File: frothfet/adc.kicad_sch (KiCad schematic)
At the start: 5 parts, among them U18 MCP3564R

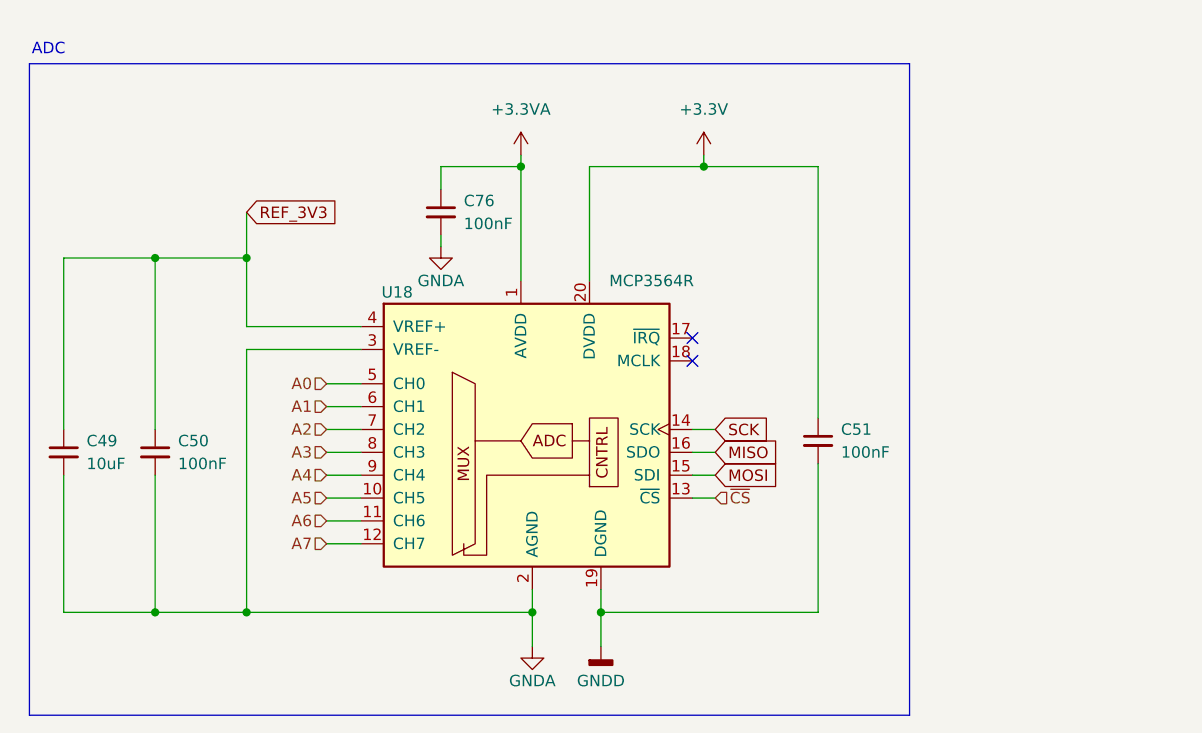
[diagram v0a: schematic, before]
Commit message: fatter power trace and layer 3 is fully ground plane now.
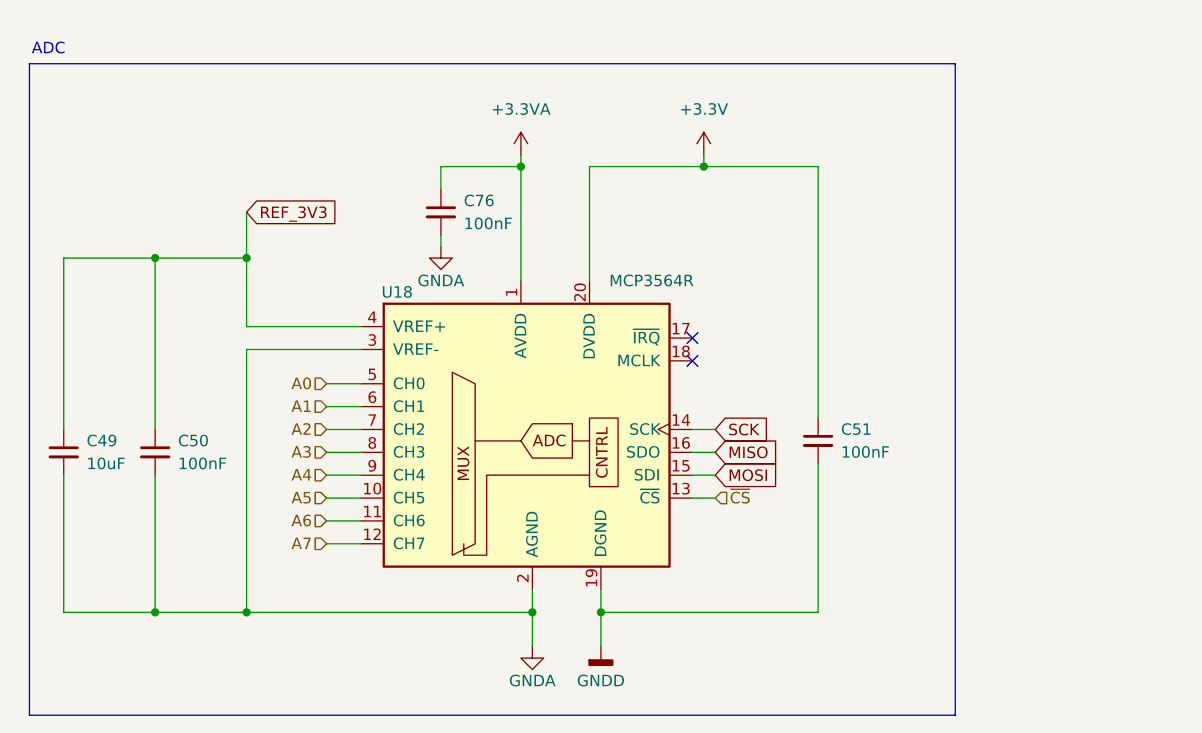
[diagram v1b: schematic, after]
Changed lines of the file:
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@@
 	(rectangle
 		(start 81.28 45.72)
-		(end 179.07 118.11)
+		(end 184.15 118.11)
 		(stroke
 			(width 0)

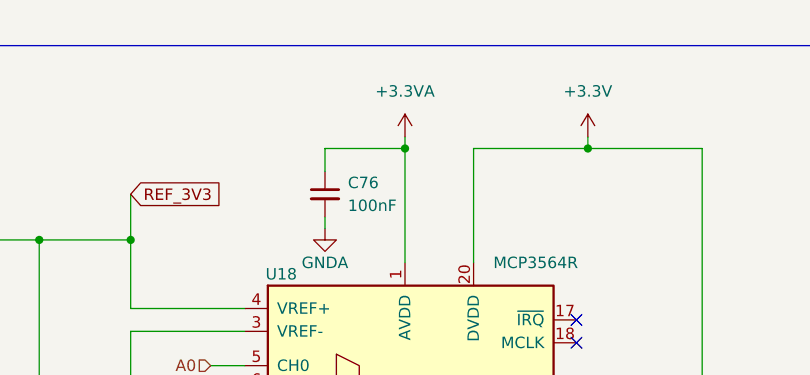
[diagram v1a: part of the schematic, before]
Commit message: added selector for 3.3VADC and finalized board.
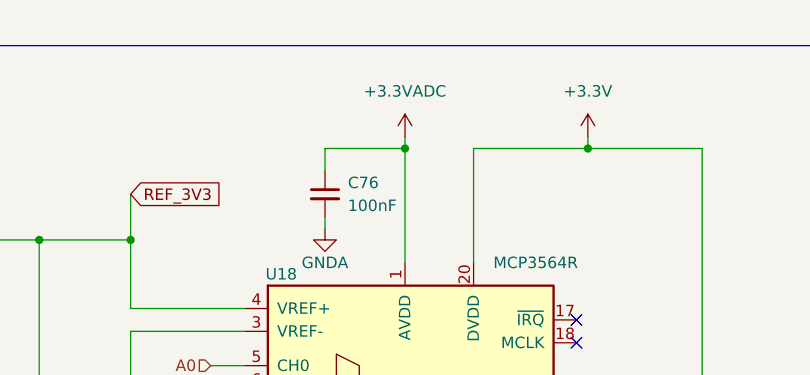
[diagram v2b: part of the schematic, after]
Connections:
- net +3.3VA renamed +3.3VADC
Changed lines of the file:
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@@
 	)
 	(symbol
-		(lib_id "power:+3.3VA")
+		(lib_id "power:+3.3VADC")
 		(at 135.89 55.88 0)
 		(unit 1)
@@
 		(fields_autoplaced yes)
 		(property "Reference" "#PWR083"
-			(at 135.89 59.69 0)
+			(at 139.7 57.15 0)
 			(effects
 				(font
@@
 			)
 		)
-		(property "Value" "+3.3VA"
+		(property "Value" "+3.3VADC"
 			(at 135.89 50.8 0)
 			(effects
@@
 			)
 		)
-		(property "Description" "Power symbol creates a global label with name \"+3.3VA\""
+		(property "Description" "Power symbol creates a global label with name \"+3.3VADC\""
 			(at 135.89 55.88 0)
 			(effects
@@
 		)
 		(instances
-			(project ""
+			(project "frothfet"
 				(path "/c83c6236-96e9-46ad-9d7a-9e2efa4a7966/b87f80e1-ecbd-4ee0-be26-4b252158928b"
 					(reference "#PWR083")

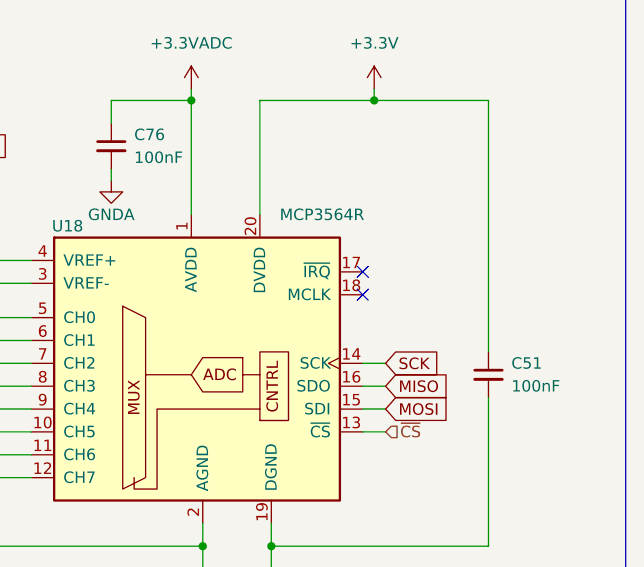
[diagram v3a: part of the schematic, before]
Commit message: added extra adc control lines
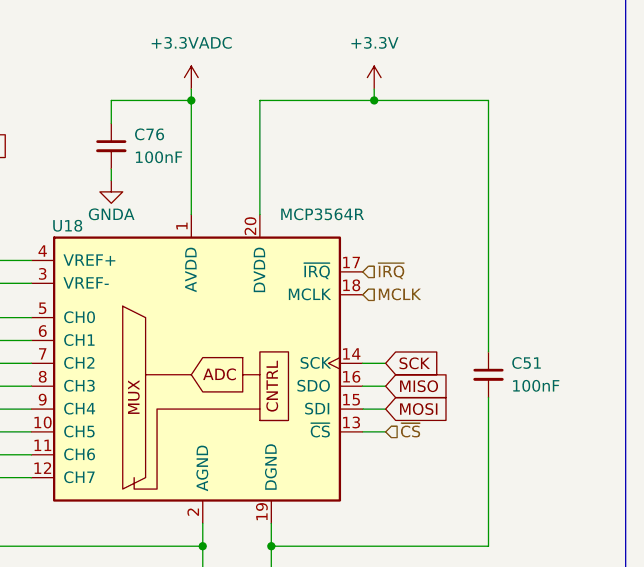
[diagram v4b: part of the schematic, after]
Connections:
- net ~{IRQ}: now reaches U18.17 (~{IRQ})
- net MCLK: now reaches U18.18 (MCLK)
- no-connect marks 2 -> 0
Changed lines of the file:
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@@
 		(color 0 0 0 0)
-	)
-	(no_connect
-		(at 154.94 78.74)
-	)
-	(no_connect
-		(at 154.94 76.2)
 	)
 	(wire
@@
 		)
 	)
+	(hierarchical_label "MCLK"
+		(shape input)
+		(at 154.94 78.74 0)
+		(fields_autoplaced yes)
+		(effects
+			(font
+				(size 1.27 1.27)
+			)
+			(justify left)
+		)
+	)
 	(hierarchical_label "A3"
 		(shape input)
@@
 		)
 	)
+	(hierarchical_label "~{IRQ}"
+		(shape input)
+		(at 154.94 76.2 0)
+		(fields_autoplaced yes)
+		(effects
+			(font
+				(size 1.27 1.27)
+			)
+			(justify left)
+		)
+	)

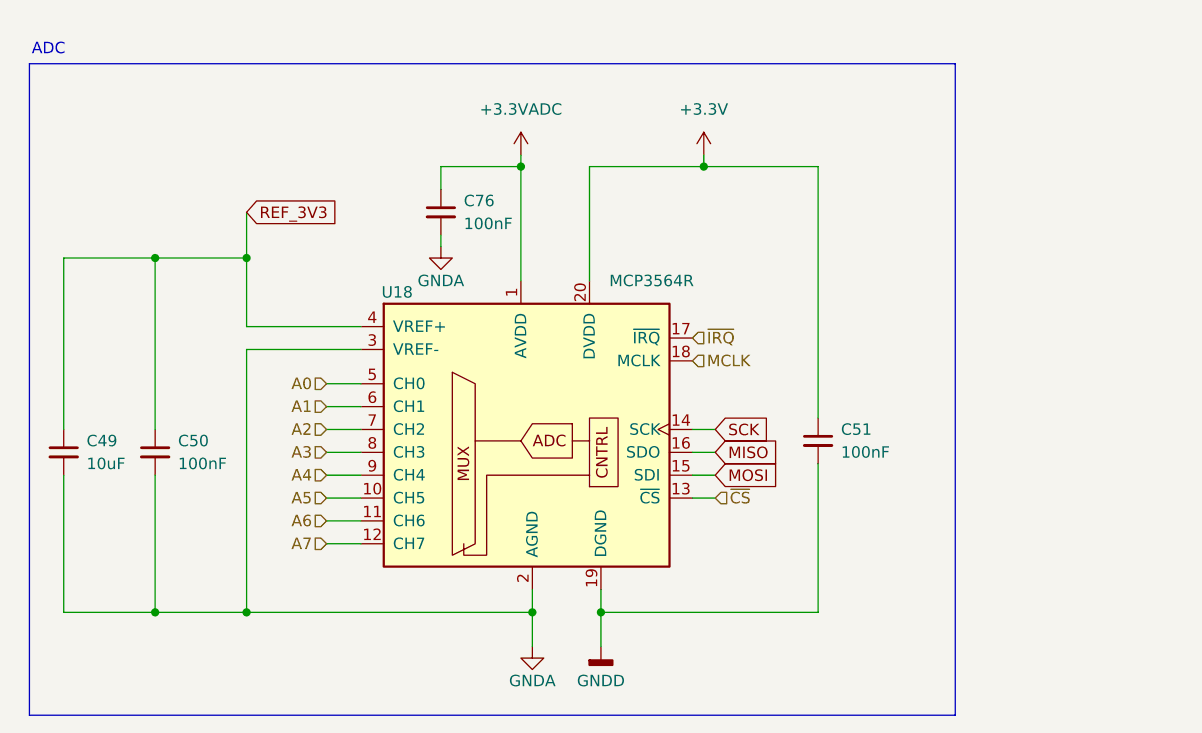
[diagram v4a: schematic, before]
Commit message: updated adc and adc power supply schematics.
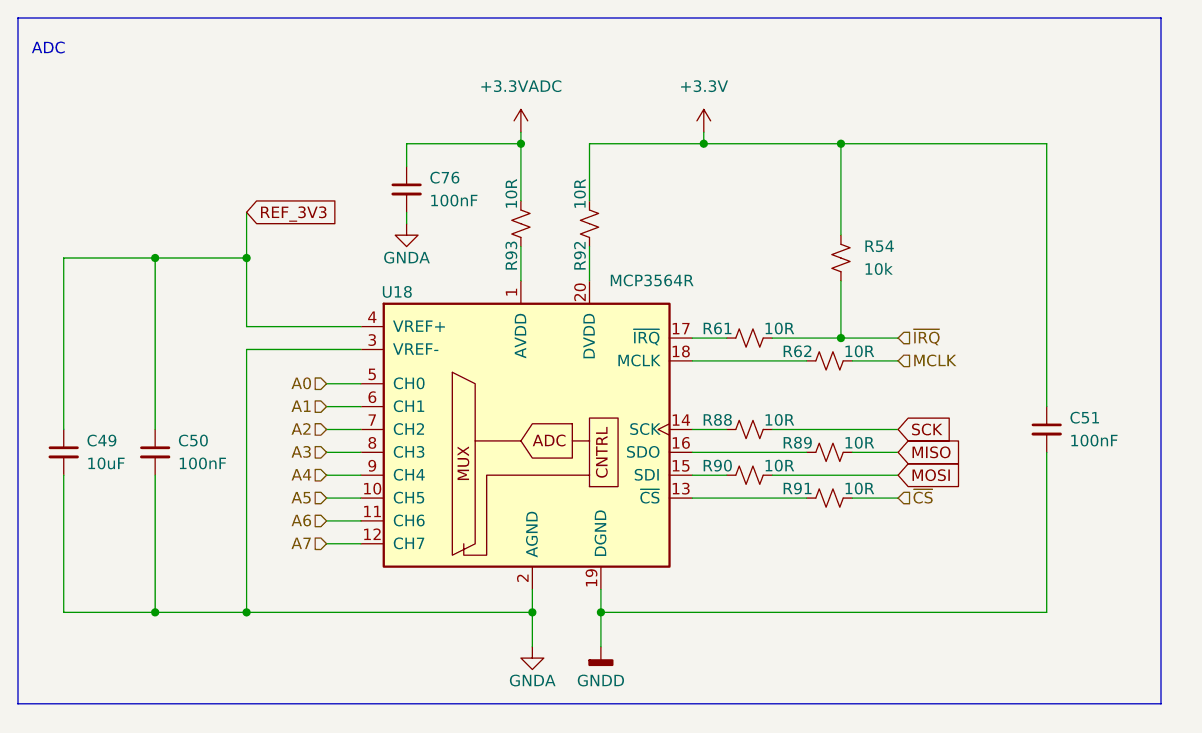
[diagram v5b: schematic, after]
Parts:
- added R54: 10k, Resistor_SMD:R_0805_2012Metric_Pad1.20x1.40mm_HandSolder, symbol Device:R_Small_US
- added R61, R62, R88, R89, R90, R91, R92, R93: 10R, Resistor_SMD:R_0805_2012Metric_Pad1.20x1.40mm_HandSolder, symbol Device:R_Small_US
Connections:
- net +3.3V: now also R54.1, R92.2; no longer U18.20 (DVDD)
- net +3.3VADC: now also R93.2; no longer U18.1 (AVDD)
- net MCLK: now also R62.2; no longer U18.18 (MCLK)
- net MISO: now also R89.2; no longer U18.16 (SDO)
- net MOSI: now also R90.2; no longer U18.15 (SDI)
- net SCK: now also R88.2; no longer U18.14 (SCK)
- net ~{CS}: now also R91.2; no longer U18.13 (~{CS})
- net ~{IRQ}: now also R54.2, R61.2; no longer U18.17 (~{IRQ})
- new net: R89.1, U18.16 (SDO)
- new net: R88.1, U18.14 (SCK)
- new net: R93.1, U18.1 (AVDD)
- new net: R90.1, U18.15 (SDI)
- new net: R61.1, U18.17 (~{IRQ})
- new net: R92.1, U18.20 (DVDD)
- new net: R62.1, U18.18 (MCLK)
- new net: R91.1, U18.13 (~{CS})
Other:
- moved on the sheet: C51, C76

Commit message: updates
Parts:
- added C79: 100nF, Capacitor_SMD:C_0805_2012Metric_Pad1.18x1.45mm_HandSolder, symbol Device:C_Small
- C51: value 100nF -> 10uF
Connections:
- net +3.3V: now also C79.1
- net GNDD: now also C79.2
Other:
- moved on the sheet: C51
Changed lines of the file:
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@@
+	)
+	(junction
+		(at 104.14 74.93)
+		(diameter 0)
+		(color 0 0 0 0)
+	)
+	(junction
+		(at 187.96 106.68)
+		(diameter 0)
+		(color 0 0 0 0)
 	)
 	(junction
@@
 	)
 	(junction
-		(at 105.41 67.31)
+		(at 95.25 74.93)
 		(diameter 0)
 		(color 0 0 0 0)
 	)
 	(junction
-		(at 95.25 67.31)
+		(at 187.96 54.61)
 		(diameter 0)
 		(color 0 0 0 0)
@@
 	(wire
 		(pts
+			(xy 187.96 106.68) (xy 199.39 106.68)
+		)
+		(stroke
+			(width 0)
+			(type default)
+		)
+	)
+	(wire
+		(pts
 			(xy 171.45 76.2) (xy 177.8 76.2)
 		)
@@
 	(wire
 		(pts
-			(xy 105.41 67.31) (xy 105.41 74.93)
-		)
-		(stroke
-			(width 0)
-			(type default)
-		)
-	)
-	(wire
-		(pts
 			(xy 118.11 77.47) (xy 105.41 77.47)
 		)
@@
 	(wire
 		(pts
-			(xy 95.25 67.31) (xy 95.25 86.36)
-		)
-		(stroke
-			(width 0)
-			(type default)
-		)
-	)
-	(wire
-		(pts
 			(xy 167.64 88.9) (xy 154.94 88.9)
 		)
@@
 	(wire
 		(pts
+			(xy 95.25 74.93) (xy 95.25 86.36)
+		)
+		(stroke
+			(width 0)
+			(type default)
+		)
+	)
+	(wire
+		(pts
 			(xy 158.75 86.36) (xy 154.94 86.36)
 		)
@@
 	(wire
 		(pts
-			(xy 95.25 67.31) (xy 85.09 67.31)
+			(xy 95.25 74.93) (xy 85.09 74.93)
 		)
 		(stroke
@@
 	(wire
 		(pts
+			(xy 187.96 88.9) (xy 187.96 106.68)
+		)
+		(stroke
+			(width 0)
+			(type default)
+		)
+	)
+	(wire
+		(pts
 			(xy 158.75 91.44) (xy 154.94 91.44)
 		)
@@
 	(wire
 		(pts
-			(xy 105.41 62.23) (xy 105.41 67.31)
-		)
-		(stroke
-			(width 0)
-			(type default)
-		)
-	)
-	(wire
-		(pts
-			(xy 144.78 106.68) (xy 194.31 106.68)
+			(xy 144.78 106.68) (xy 187.96 106.68)
 		)
 		(stroke
@@
 	(wire
 		(pts
-			(xy 105.41 67.31) (xy 95.25 67.31)
+			(xy 104.14 74.93) (xy 118.11 74.93)
 		)
 		(stroke
@@
 	(wire
 		(pts
-			(xy 85.09 67.31) (xy 85.09 86.36)
-		)
-		(stroke
-			(width 0)
-			(type default)
-		)
-	)
-	(wire
-		(pts
-			(xy 105.41 74.93) (xy 118.11 74.93)
+			(xy 104.14 54.61) (xy 104.14 74.93)
+		)
+		(stroke
+			(width 0)
+			(type default)
+		)
+	)
+	(wire
+		(pts
+			(xy 85.09 74.93) (xy 85.09 86.36)
 		)
 		(stroke
@@
 	(wire
 		(pts
+			(xy 187.96 54.61) (xy 187.96 83.82)
+		)
+		(stroke
+			(width 0)
+			(type default)
+		)
+	)
+	(wire
+		(pts
 			(xy 118.11 96.52) (xy 114.3 96.52)
 		)
@@
 	(wire
 		(pts
+			(xy 104.14 74.93) (xy 95.25 74.93)
+		)
+		(stroke
+			(width 0)
+			(type default)
+		)
+	)
+	(wire
+		(pts
 			(xy 105.41 106.68) (xy 137.16 106.68)
 		)
@@
 	(wire
 		(pts
-			(xy 194.31 106.68) (xy 194.31 88.9)
+			(xy 199.39 106.68) (xy 199.39 88.9)
 		)
 		(stroke
@@
 	(wire
 		(pts
-			(xy 171.45 54.61) (xy 194.31 54.61)
+			(xy 171.45 54.61) (xy 187.96 54.61)
 		)
 		(stroke
@@
 	(wire
 		(pts
+			(xy 187.96 54.61) (xy 199.39 54.61)
+		)
+		(stroke
+			(width 0)
+			(type default)
+		)
+	)
+	(wire
+		(pts
 			(xy 118.11 99.06) (xy 114.3 99.06)
 		)
@@
 	(wire
 		(pts
-			(xy 194.31 54.61) (xy 194.31 83.82)
+			(xy 199.39 54.61) (xy 199.39 83.82)
 		)
 		(stroke
@@
 	(rectangle
 		(start 80.01 40.64)
-		(end 207.01 116.84)
+		(end 209.55 116.84)
 		(stroke
 			(width 0)
@@
 	(global_label "REF_3V3"
 		(shape input)
-		(at 105.41 62.23 0)
+		(at 104.14 54.61 90)
 		(fields_autoplaced yes)
 		(effects
@@
 		)
 		(property "Intersheetrefs" "${INTERSHEET_REFS}"
-			(at 116.378 62.23 0)
+			(at 104.14 43.642 90)
 			(effects
 				(font
@@
 	(symbol
 		(lib_id "Device:C_Small")
-		(at 194.31 86.36 0)
+		(at 199.39 86.36 0)
 		(unit 1)
 		(exclude_from_sim no)
@@
 		(dnp no)
 		(property "Reference" "C51"
-			(at 196.85 85.0963 0)
+			(at 201.93 85.0963 0)
 			(effects
 				(font
@@
 			)
 		)
-		(property "Value" "100nF"
-			(at 196.85 87.6363 0)
+		(property "Value" "10uF"
+			(at 201.93 87.6363 0)
 			(effects
 				(font
@@
 		)
 		(property "Footprint" "Capacitor_SMD:C_0805_2012Metric_Pad1.18x1.45mm_HandSolder"
-			(at 194.31 86.36 0)
+			(at 199.39 86.36 0)
 			(effects
 				(font
@@
 		)
 		(property "Datasheet" "~"
-			(at 194.31 86.36 0)
+			(at 199.39 86.36 0)
 			(effects
 				(font
@@
 		)
 		(property "Description" ""
-			(at 194.31 86.36 0)
+			(at 199.39 86.36 0)
 			(effects
 				(font
@@
 		)
 		(property "Mouser" ""
-			(at 194.31 86.36 0)
+			(at 199.39 86.36 0)
 			(effects
 				(font
@@
 		)
 		(property "LCSC" "C49678"
-			(at 194.31 86.36 0)
+			(at 199.39 86.36 0)
 			(effects
 				(font
@@
 		)
 		(property "ALT" ""
-			(at 194.31 86.36 0)
+			(at 199.39 86.36 0)
 			(effects
 				(font
@@
 					(unit 1)
 				)
+			)
+		)
+	)
+	(symbol
+		(lib_id "Device:C_Small")
+		(at 187.96 86.36 0)
+		(unit 1)
+		(exclude_from_sim no)
+		(in_bom yes)
+		(on_board yes)
+		(dnp no)
+		(property "Reference" "C79"
+			(at 190.5 85.0963 0)
+			(effects
+				(font
+					(size 1.27 1.27)
+				)
+				(justify left)
+			)
+		)
+		(property "Value" "100nF"
+			(at 190.5 87.6363 0)
+			(effects
+				(font
+					(size 1.27 1.27)
+				)
+				(justify left)
+			)
+		)
+		(property "Footprint" "Capacitor_SMD:C_0805_2012Metric_Pad1.18x1.45mm_HandSolder"
+			(at 187.96 86.36 0)
+			(effects
+				(font
+					(size 1.27 1.27)
+				)
+				(hide yes)
+			)
+		)
+		(property "Datasheet" "~"
+			(at 187.96 86.36 0)
+			(effects
+				(font
+					(size 1.27 1.27)
+				)
+				(hide yes)
+			)
+		)
+		(property "Description" ""
+			(at 187.96 86.36 0)
+			(effects
+				(font
+					(size 1.27 1.27)
+				)
+				(hide yes)
+			)
+		)
+		(property "Mouser" ""
+			(at 187.96 86.36 0)
+			(effects
+				(font
+					(size 1.27 1.27)
+				)
+				(hide yes)
+			)
+		)
+		(property "LCSC" "C49678"
+			(at 187.96 86.36 0)
+			(effects
+				(font
+					(size 1.27 1.27)
+				)
+				(hide yes)
+			)
+		)
+		(property "ALT" ""
+			(at 187.96 86.36 0)
+			(effects
+				(font
+					(size 1.27 1.27)
+				)
+				(hide yes)
+			)
+		)
+		(pin "1"
+		)
+		(pin "2"
+		)
+		(instances
+			(project "frothfet"
+				(path "/c83c6236-96e9-46ad-9d7a-9e2efa4a7966/b87f80e1-ecbd-4ee0-be26-4b252158928b"
+					(reference "C79")
+					(unit 1)
+				)
